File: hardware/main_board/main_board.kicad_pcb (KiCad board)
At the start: 4 copper layers, 225.9 x 135 mm, 87 parts, among them J1 +5v in, J10 uart, J11 input 4, J12 input 5, J14 +5v in/out, J16 input 6, J17 input 7, J19 rgb output, J20 ypbpr output, J3 input 0, J4 input 1, J5 icsp, J7 input 2, J8 input 3, SW1 rgb/ypbpr, SW10 prev, SW11 next, SW12 csync/rgbs, SW13 csync/rgbs, SW14 csync/rgbs, SW15 csync/rgbs, SW16 csync/rgbs, SW17 csync/rgbs, SW18 csync/rgbs, SW19 csync/rgbs, SW2 rgb/ypbpr, SW20 csync/rgbs, SW3 rgb/ypbpr, SW4 rgb/ypbpr, SW5 rgb/ypbpr, SW6 rgb/ypbpr, SW7 rgb/ypbpr, SW8 rgb/ypbpr, U1 ATmega328PB-A, U10 SN74CBT3244CPW, U11 SN74CBT3244CPW, U12 SN74CBT3244CPW, U13 SN74CBT3244CPW, U14 74HC238, U15 74HC238, U3 SN74CBT3244CPW, U4 SN74CBT3244CPW, U5 74HC138, U6 74HC04, U7 SN74CBT3244CPW, U8 SN74CBT3244CPW, U9 SN74CBT3244CPW

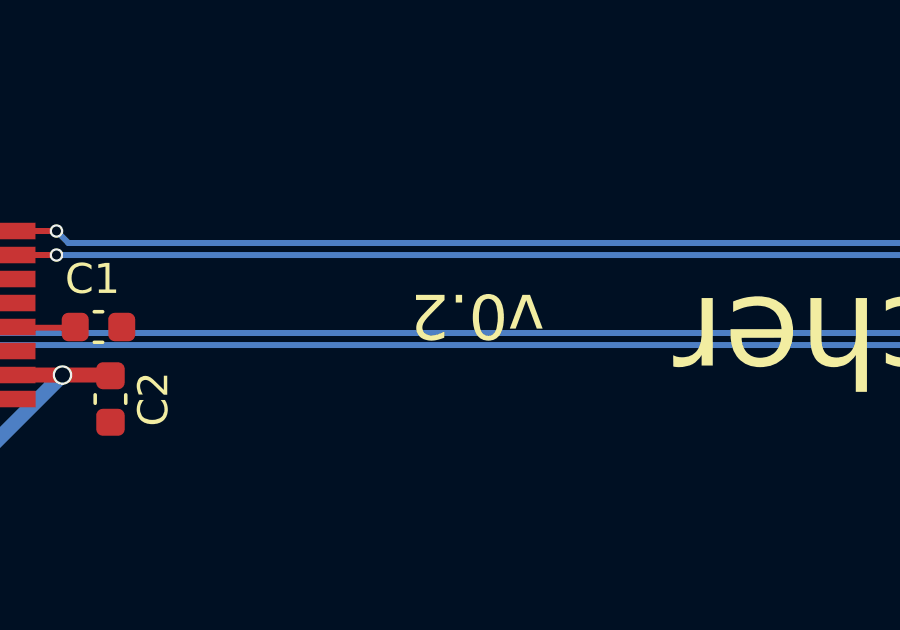
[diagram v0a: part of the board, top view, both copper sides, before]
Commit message: #5: Upversioned the board finally! Migrated BOM format to use "KiCAD JLCPCB tools" plugin. Updated hardware README.md.
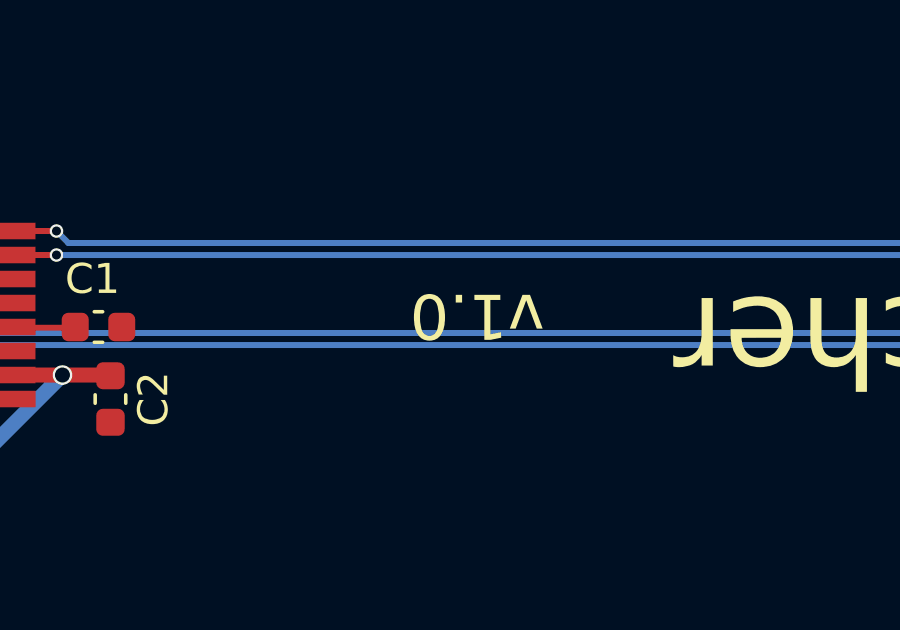
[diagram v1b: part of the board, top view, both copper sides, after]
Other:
- board text added: "v1.0"
- board text removed: "v0.2"
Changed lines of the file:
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@@
 	(title_block
 		(title "MO-011 rgb switcher (main board)")
-		(date "2025-01-21")
-		(rev "v0.2")
+		(date "2026-03-16")
+		(rev "v1.0")
 	)
 	(layers
@@
 		(sheetname "/")
 		(sheetfile "main_board.kicad_sch")
-		(attr through_hole)
+		(attr through_hole exclude_from_pos_files)
 		(fp_line
 			(start 11 1.5)
@@
 		(sheetname "/")
 		(sheetfile "main_board.kicad_sch")
-		(attr through_hole)
+		(attr through_hole exclude_from_pos_files)
 		(fp_line
 			(start 11 1.5)
@@
 		(sheetname "/")
 		(sheetfile "main_board.kicad_sch")
-		(attr through_hole)
+		(attr through_hole exclude_from_pos_files)
 		(fp_line
 			(start 11 1.5)
@@
 		(sheetname "/")
 		(sheetfile "main_board.kicad_sch")
-		(attr through_hole)
+		(attr through_hole exclude_from_pos_files)
 		(fp_line
 			(start 11 1.5)
@@
 		(sheetname "/")
 		(sheetfile "main_board.kicad_sch")
-		(attr through_hole)
+		(attr through_hole exclude_from_pos_files)
 		(fp_line
 			(start 11 1.5)
@@
 		(sheetname "/")
 		(sheetfile "main_board.kicad_sch")
-		(attr through_hole)
+		(attr through_hole exclude_from_pos_files exclude_from_bom)
 		(fp_line
 			(start 3.87 -1.33)
@@
 		(embedded_fonts no)
 		(model "${KICAD8_3DMODEL_DIR}/Connector_PinHeader_2.54mm.3dshapes/PinHeader_2x03_P2.54mm_Vertical.wrl"
+			(hide yes)
 			(offset
 				(xyz 0 0 0)
@@
 		(sheetname "/")
 		(sheetfile "main_board.kicad_sch")
-		(attr through_hole)
+		(attr through_hole exclude_from_pos_files)
 		(fp_line
 			(start 11 1.5)
@@
 		(sheetname "/")
 		(sheetfile "main_board.kicad_sch")
-		(attr through_hole)
+		(attr through_hole exclude_from_pos_files)
 		(fp_line
 			(start 11 1.5)
@@
 		(sheetname "/")
 		(sheetfile "main_board.kicad_sch")
-		(attr through_hole)
+		(attr through_hole exclude_from_pos_files)
 		(fp_line
 			(start 11 1.5)
@@
 		(sheetname "/")
 		(sheetfile "main_board.kicad_sch")
-		(attr through_hole)
+		(attr through_hole exclude_from_pos_files)
 		(fp_line
 			(start 11 1.5)
@@
 		(sheetname "/")
 		(sheetfile "main_board.kicad_sch")
-		(attr through_hole)
+		(attr through_hole exclude_from_pos_files)
 		(fp_line
 			(start 11 1.5)
@@
 		)
 	)
-	(gr_text "v0.2"
+	(gr_text "v1.0"
 		(at 188.467892 70.421602 180)
 		(layer "F.SilkS")

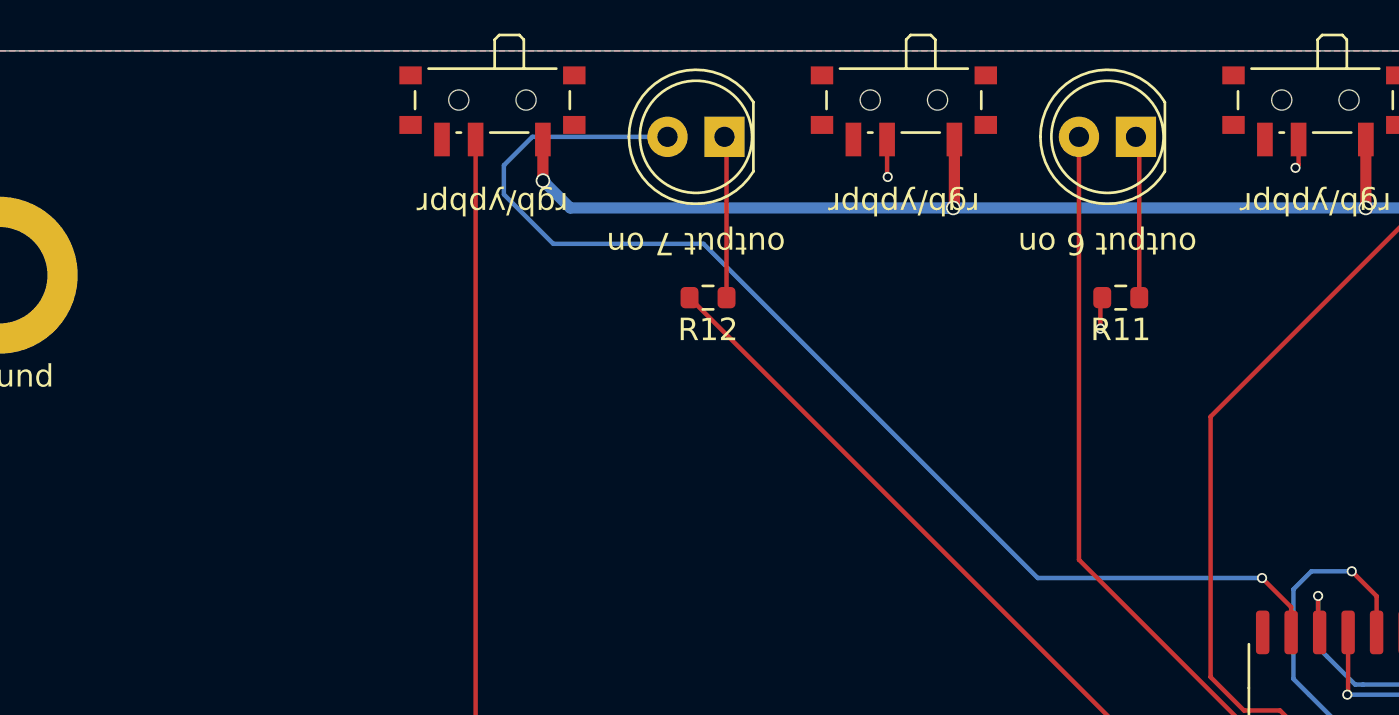
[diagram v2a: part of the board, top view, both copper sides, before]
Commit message: #5: Fixed dumb mistake I made where I got rid of the power LED!
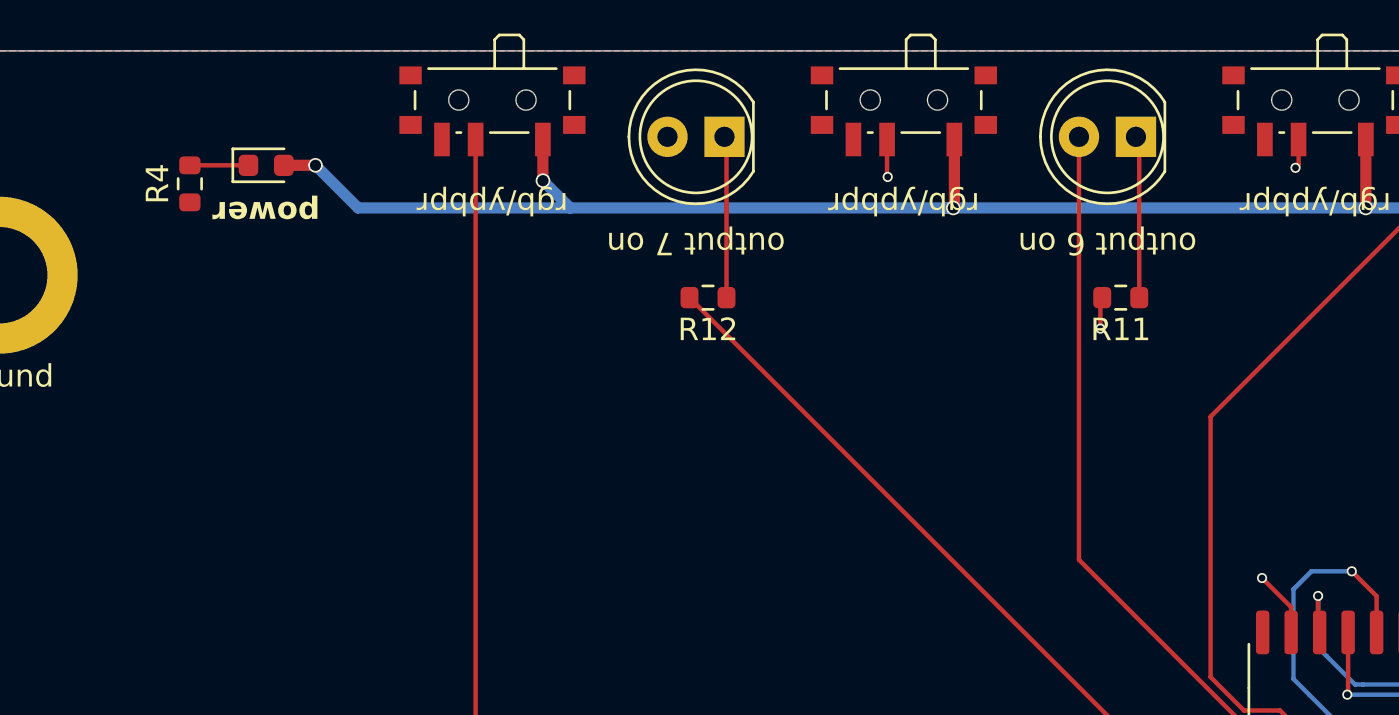
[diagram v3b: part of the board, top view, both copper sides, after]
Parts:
- added D1: power, LED_SMD:LED_0603_1608Metric, F.Cu at (57.7, 28.5)
- added R4: 6k8, Resistor_SMD:R_0603_1608Metric, F.Cu at (54.3, 29.3)
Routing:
- net +5V: track 705.9 -> 719.4 mm, vias 23 -> 24
- net RGBIsSelected7: track 53.0 -> 43.1 mm
- net Net-(D1-K): track 0.00 -> 2.61 mm
